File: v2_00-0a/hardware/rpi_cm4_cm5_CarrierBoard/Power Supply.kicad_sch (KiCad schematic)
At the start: 84 parts, among them Q7 2N7002, Q8 2N7002, Q9 DMPH6050SK3-13, U10 TLV62130ARGTR, U11 TLV62130ARGTR, U12 TPS7A7002DDAR, U13 SE555DR, U14 SN74LVC1G14DBVR, U9 TLV62130ARGTR

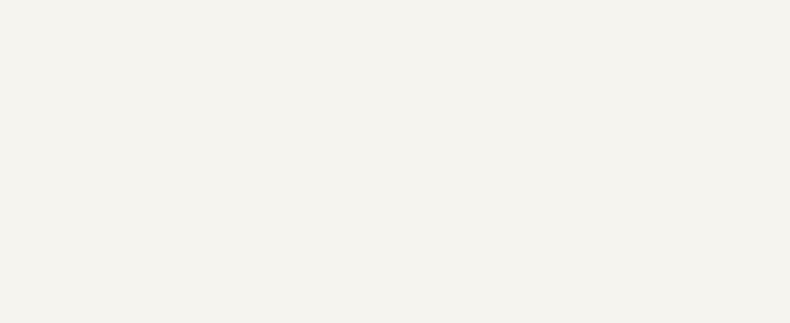
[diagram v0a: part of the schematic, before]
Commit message: Add schematic pages for SOM_CONN_A/B, DSI to LVDS bridge, Ethernet and HDMI
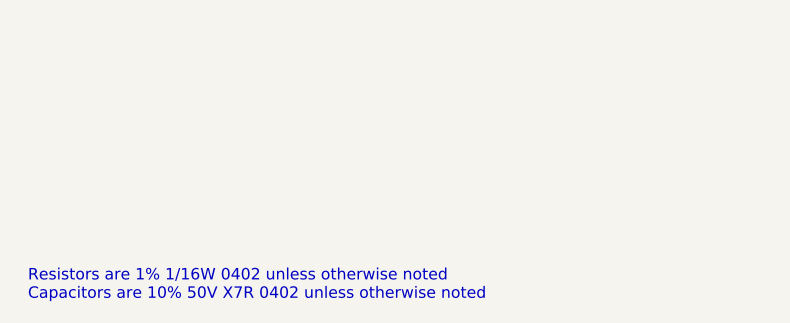
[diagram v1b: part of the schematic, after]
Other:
- note added: "Resistors are 1% 1/16W 0402 unless otherwise noted Capacitors are 10% 50V X7R 0402 unless otherwise noted"
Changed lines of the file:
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@@
 		(comment 8 "WIP")
+	)
+	(text "Resistors are 1% 1/16W 0402 unless otherwise noted\nCapacitors are 10% 50V X7R 0402 unless otherwise noted"
+		(exclude_from_sim no)
+		(at 13.208 170.434 0)
+		(effects
+			(font
+				(size 1.27 1.27)
+			)
+			(justify left)
+		)
 	)
 	(junction

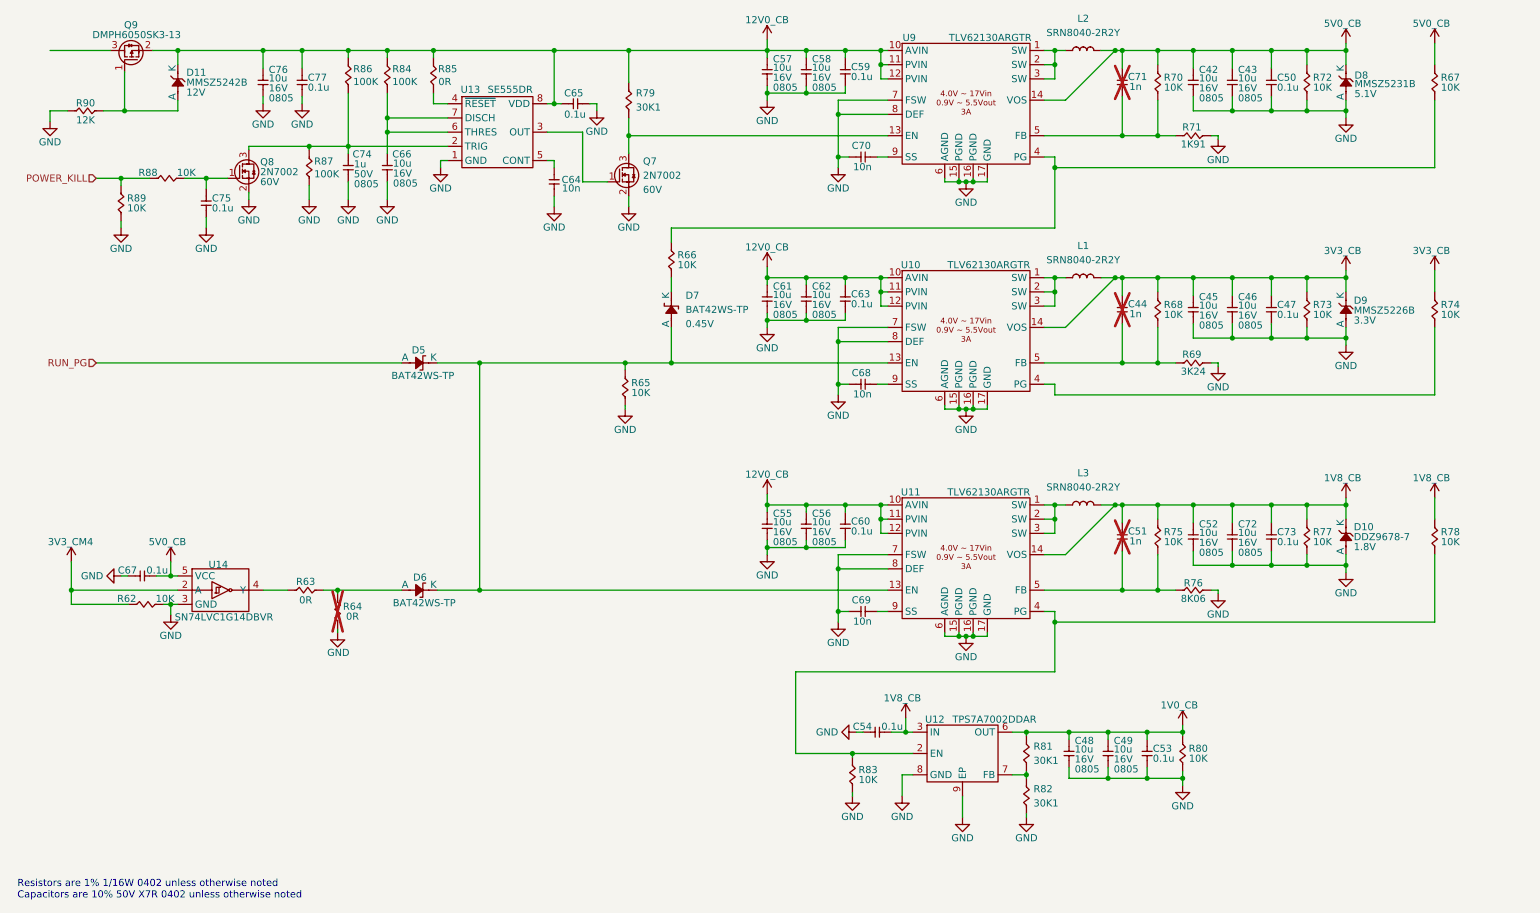
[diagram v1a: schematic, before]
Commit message: Add new page and update schematics
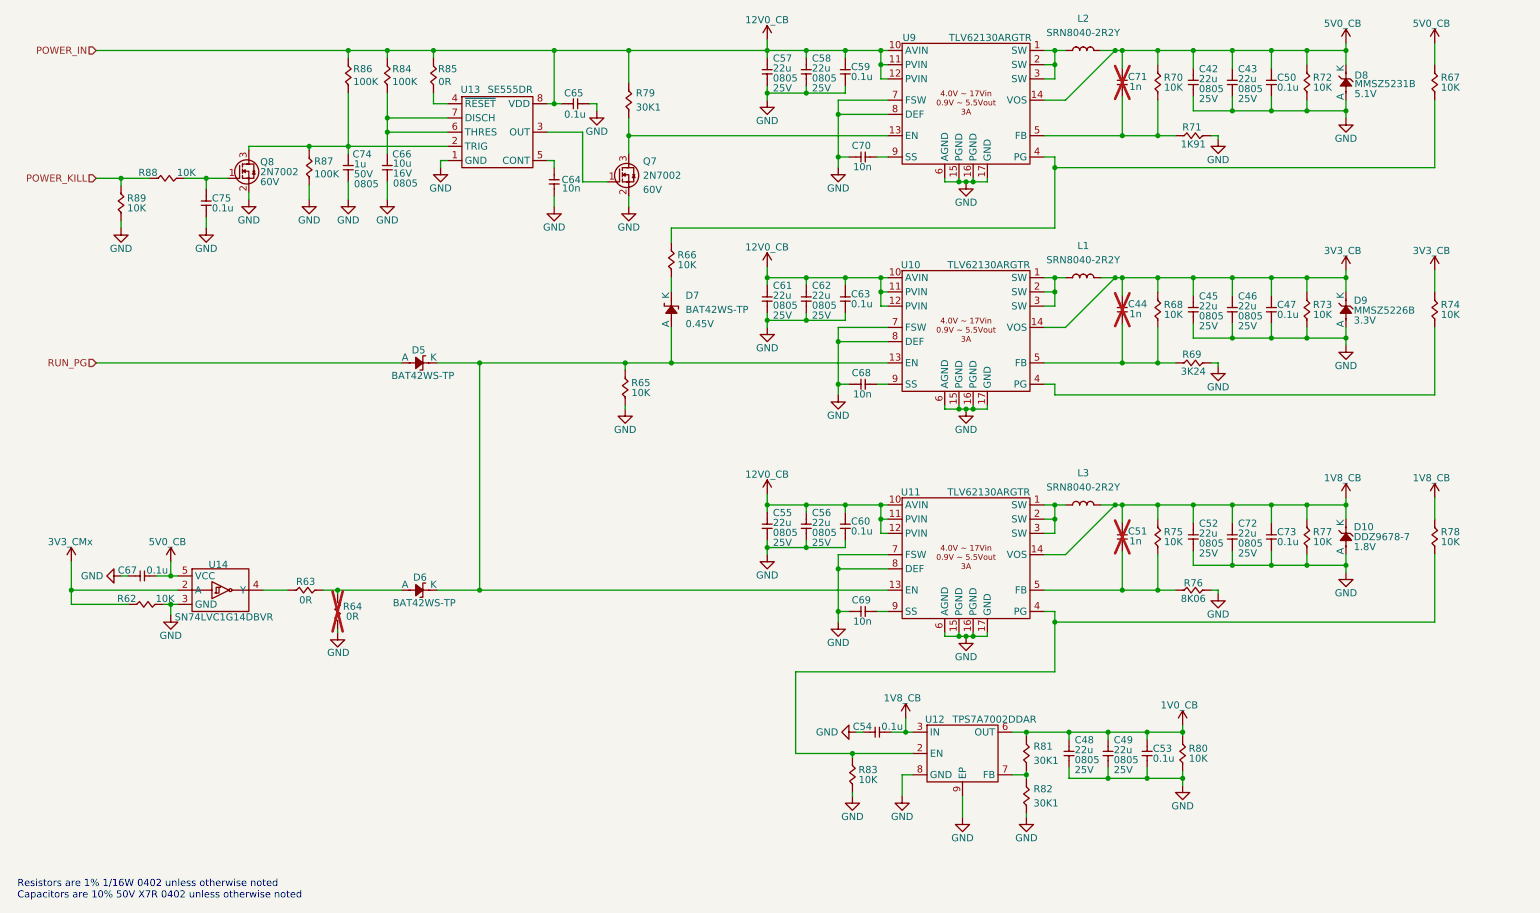
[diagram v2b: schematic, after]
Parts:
- removed C42, C43, C45, C46, C48, C49, C52, C55, C56, C57, C58, C61, C62, C72, C76: 10u, footprint:CAP_NONPOL_0805, symbol KicadCompDb:Capacitors/CAP_CER_SMT_00004
- removed C77: 0.1u, footprint:CAP_NONPOL_0402, symbol KicadCompDb:Capacitors/CAP_CER_SMT_00001
- removed D11: MMSZ5242B, footprint:SOD-123, symbol KicadCompDb:Diodes/DIODE_00003
- removed Q9: DMPH6050SK3-13, footprint:TO-252-3, symbol KicadCompDb:Mosfet/MOSFET_00003
- removed R90: 12K, footprint:RES_0402, symbol KicadCompDb:Resistors/RES_SMT_00014
- added C42, C43, C45, C46, C48, C49, C52, C55, C56, C57, C58, C61, C62, C72: 22u, footprint:CAP_NONPOL_0805, symbol KicadCompDb:Capacitors/CAP_CER_SMT_00011
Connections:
- net 12V0_CB: now also C55.2, C56.2, C57.2, C58.2, C61.2, C62.2
- net 1V0_CB: now also C48.2, C49.2
- net 1V8_CB: now also C52.2, C72.2
- net 3V3_CB: now also C45.2, C46.2
- net 5V0_CB: now also C42.2, C43.2
- net GND: now also C42.1, C43.1, C45.1, C46.1, C48.1, C49.1, C52.1, C55.1, C56.1, C57.1, C58.1, C61.1, C62.1, C72.1
- net 3V3_CM4 renamed 3V3_CMx

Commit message: Add design notes (power table) and latest changes to power supply and power input
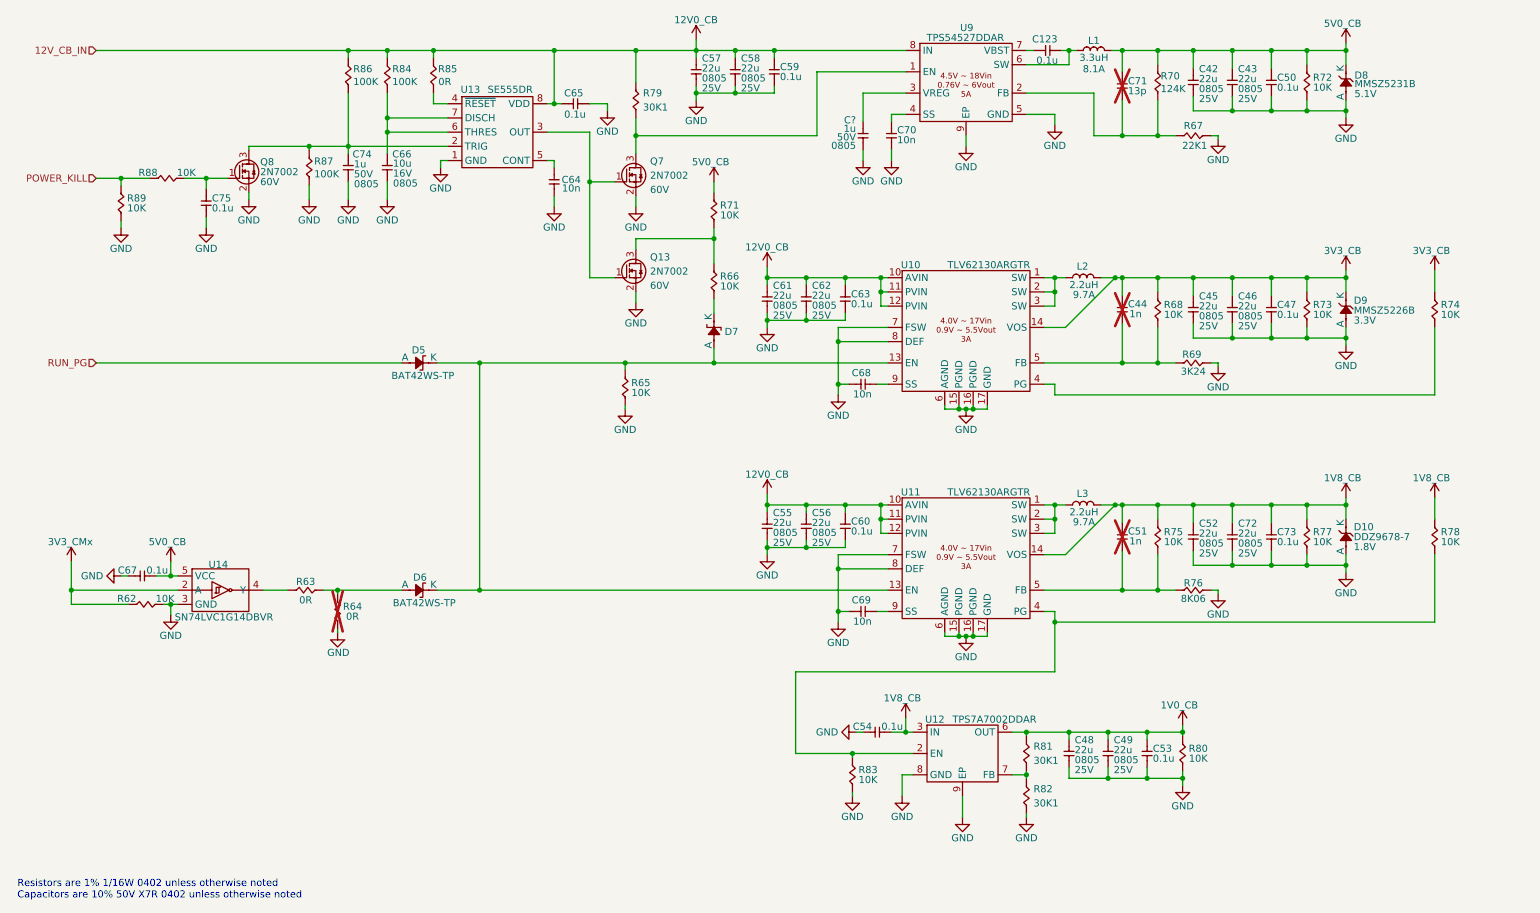
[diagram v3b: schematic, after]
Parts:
- removed C71: 1n, footprint:CAP_NONPOL_0402, symbol KicadCompDb:Capacitors/CAP_CER_SMT_00005
- removed L1, L2, L3: SRN8040-2R2Y, footprint:SRN8040, symbol KicadCompDb:Inductor/IND_00001
- removed R67, R70: 10K, footprint:RES_0402, symbol KicadCompDb:Resistors/RES_SMT_00013
- removed R71: 1K91, footprint:RES_0402, symbol KicadCompDb:Resistors/RES_SMT_00005
- removed U9: TLV62130ARGTR, footprint:VQFN-16-EP, symbol KicadCompDb:Regulator/REG_00001
- added C123: 0.1u, footprint:CAP_NONPOL_0402, symbol KicadCompDb:Capacitors/CAP_CER_SMT_00001
- added C71: 13p, footprint:CAP_NONPOL_0402, symbol KicadCompDb:Capacitors/CAP_CER_SMT_00003
- added C?: 1u, footprint:CAP_NONPOL_0805, symbol KicadCompDb:Capacitors/CAP_CER_SMT_00002
- added L1: PA5003.332NLT, footprint:PA5003, symbol KicadCompDb:Inductor/IND_00006
- added L2, L3: PA5003.222NLT, footprint:PA5003, symbol KicadCompDb:Inductor/IND_00007
- added Q13: 2N7002, footprint:SOT-23-3, symbol KicadCompDb:Mosfet/MOSFET_00001
- added R67: 22K1, footprint:RES_0402, symbol KicadCompDb:Resistors/RES_SMT_00023
- added R70: 124K, footprint:RES_0402, symbol KicadCompDb:Resistors/RES_SMT_00024
- added R71: 10K, footprint:RES_0402, symbol KicadCompDb:Resistors/RES_SMT_00013
- added U9: TPS54527DDAR, footprint:SO-8-150mil-EP, symbol KicadCompDb:Regulator/REG_00009
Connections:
- net 12V0_CB: now also U9.8 (IN)
- net 1V8_CB: now also L3.2
- net 3V3_CB: now also L2.2
- net 5V0_CB: now also C71.2, L1.2, R70.2, R71.2
- net GND: now also C70.1, C?.1, Q13.2 (S), R67.2, U9.5 (GND), U9.9 (EP); no longer C70.2
- net at U11.1 (SW), U11.2 (SW), U11.3 (SW): now also L3.1
- net at U10.1 (SW), U10.2 (SW), U10.3 (SW): now also L2.1
- net at R66.2: now also Q13.3 (D), R71.1
- net at Q7.3 (D), R79.1: now also U9.1 (EN)
- net at Q7.1 (G), U13.3 (OUT): now also Q13.1 (G)
- new net: C123.1, L1.1, U9.6 (SW)
- new net: C123.2, U9.7 (VBST)
- new net: C71.1, R67.1, R70.1, U9.2 (FB)
- new net: C70.2, U9.4 (SS)
- new net: C?.2, U9.3 (VREG)
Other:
- moved on the sheet: C57, C58, C59, D7, Q7, R66, R79

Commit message: Add and modify existing schematics
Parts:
- removed C44, C51: 1n, footprint:CAP_NONPOL_0402, symbol KicadCompDb:Capacitors/CAP_CER_SMT_00005
- removed C68, C69: 10n, footprint:CAP_NONPOL_0402, symbol KicadCompDb:Capacitors/CAP_CER_SMT_00008
- removed C?: 1u, footprint:CAP_NONPOL_0805, symbol KicadCompDb:Capacitors/CAP_CER_SMT_00002
- removed L3: PA5003.222NLT, footprint:PA5003, symbol KicadCompDb:Inductor/IND_00007
- removed R65, R74, R75, R78: 10K, footprint:RES_0402, symbol KicadCompDb:Resistors/RES_SMT_00013
- removed R69: 3K24, footprint:RES_0402, symbol KicadCompDb:Resistors/RES_SMT_00009
- removed R76: 8K06, footprint:RES_0402, symbol KicadCompDb:Resistors/RES_SMT_00012
- removed R81: 30K1, footprint:RES_0402, symbol KicadCompDb:Resistors/RES_SMT_00016
- removed U10, U11: TLV62130ARGTR, footprint:VQFN-16-EP, symbol KicadCompDb:Regulator/REG_00001
- removed U12: TPS7A7002DDAR, footprint:SO-8-150mil-EP, symbol KicadCompDb:Regulator/REG_00007
- added C167, C68, C69: 1u, footprint:CAP_NONPOL_0805, symbol KicadCompDb:Capacitors/CAP_CER_SMT_00002
- added C168, C171: 0.1u, footprint:CAP_NONPOL_0402, symbol KicadCompDb:Capacitors/CAP_CER_SMT_00001
- added C169, C170: 10n, footprint:CAP_NONPOL_0402, symbol KicadCompDb:Capacitors/CAP_CER_SMT_00008
- added C44, C51: 13p, footprint:CAP_NONPOL_0402, symbol KicadCompDb:Capacitors/CAP_CER_SMT_00003
- added L3: PA5003.152NLT, footprint:PA5003, symbol KicadCompDb:Inductor/IND_00009
- added R65: 100K, footprint:RES_0402, symbol KicadCompDb:Resistors/RES_SMT_00018
- added R69, R74: 22K1, footprint:RES_0402, symbol KicadCompDb:Resistors/RES_SMT_00023
- added R75: 30K1, footprint:RES_0402, symbol KicadCompDb:Resistors/RES_SMT_00016
- added R81: 33K, footprint:RES_0402, symbol KicadCompDb:Resistors/RES_SMT_00031
- added U10, U11: TPS54527DDAR, footprint:SO-8-150mil-EP, symbol KicadCompDb:Regulator/REG_00009
- added U12: TPS7A7001DDAR, footprint:SO-8-150mil-EP, symbol KicadCompDb:Regulator/REG_00008
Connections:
- net 12V0_CB: now also U10.8 (IN), U11.8 (IN)
- net 1V8_CB: now also R83.2, C51.2, L3.2, R75.2, U12.2 (EN), U12.3 (IN)
- net 3V3_CB: now also C44.2
- net GND: now also C167.1, C169.1, C170.1, C68.1, C69.1, R65.1, R69.2, R74.2, U10.5 (GND), U10.9 (EP), U11.5 (GND), U11.9 (EP), U12.8 (GND), U12.9 (EP)
- net PWR_LOG_EN: now reaches D5.1 (K), D6.1 (K), D7.2 (A)
- net PWR_LOG_EN: now also R65.2, U10.1 (EN), U11.1 (EN)
- net at L2.1: now also C168.1, U10.6 (SW)
- net at R68.1: now also C44.1, R69.1, U10.2 (FB)
- net at R82.2: now also R81.1, U12.7 (FB)
- net at U9.3 (VREG): now also C167.2
- net 1V0_CB renamed 1V05_CB
- net 1V05_CB: now also R81.2, U12.6 (OUT)
- new net: C68.2, U10.3 (VREG)
- new net: C169.2, U10.4 (SS)
- new net: C168.2, U10.7 (VBST)
- new net: C69.2, U11.3 (VREG)
- new net: C170.2, U11.4 (SS)
- new net: C171.1, L3.1, U11.6 (SW)
- new net: C51.1, R74.1, R75.1, U11.2 (FB)
- new net: C171.2, U11.7 (VBST)
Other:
- note added: "1V05 ±5% 0.9975V to 1.1025V"
- note added: "1V8 ±5% 1.71V to 1.89V"
- note added: "3V3 ±5% 3.135V to 3.465V"
- note added: "5V0 ±5% 4.75V to 5.25V"
- note added: "Push-pull @ 3V3_CMx PG output of CMx PMIC"
- note added: "Release PWR_LOG_EN if 3V3_CMx not present"
- moved on the sheet: C123, C42, C43, C45, C46, C47, C48, C49, C50, C52, C53, C54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
